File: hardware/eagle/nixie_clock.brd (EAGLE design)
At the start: 199.4 x 199.4 mm, 72 parts, among them IC1 74141N, IC10 7477N, IC11 74141N, IC12 7477N, IC2 7477N, IC3 74141N, IC4 7477N, IC5 74141N, IC6 7477N, IC7 74141N, IC8 7477N, IC9 74141N, J1 RASPBERRYPI-40-PIN-GPIO, J1_180V 22-27-2021-02, J1_5V1 22-27-2021-02, J1_5V2 22-27-2021-02, K1 4052, SW1 ROTARTY_ENCODER

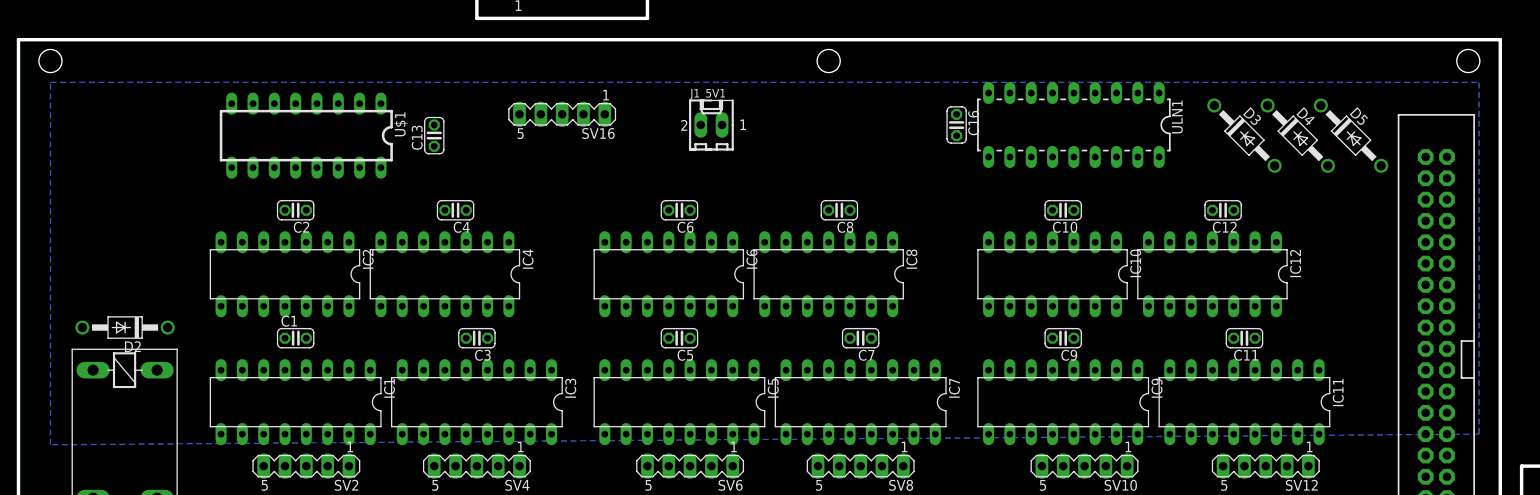
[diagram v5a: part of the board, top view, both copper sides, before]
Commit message: Fixed some issues related with the multiplexed data
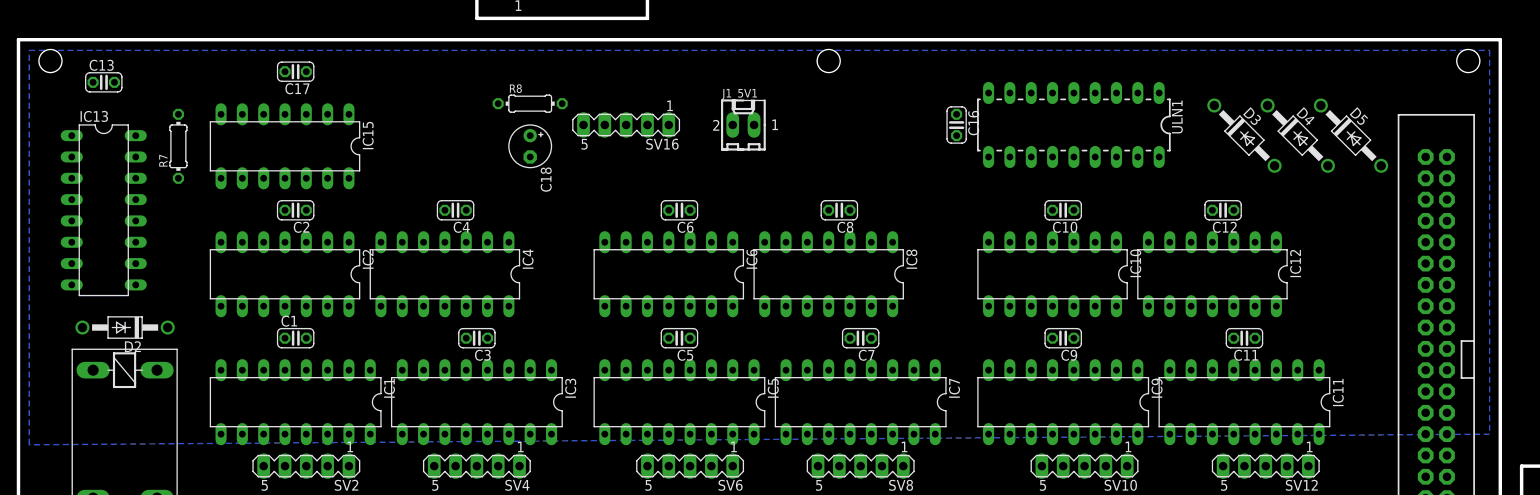
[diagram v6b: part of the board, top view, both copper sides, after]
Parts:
- removed U$1: M74HC238, SparkFun-DigitalIC:DIL16
- added C17: 100nF, resistor:C025-024X044
- added C18: 1uF, rcl:E2,5-5
- added IC13: 74HCT259N, 74xx-eu:DIL16
- added IC15: 7477N, 74xx-eu:DIL14
- added R7: 10k, rcl:0204/7
- added R8: 4k7, rcl:0204/7
- moved C13 39.9 mm to (10.2, 73.7), turned to 0 degrees
- moved SV16 7.73 mm to (72.4, 68.6)
- moved J1_5V1 3.81 mm to (86.4, 68.6)
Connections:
- removed net N$139: J1.10, ULN1.3
- new net N$141: IC15.1, J1.22
- new net N$142: IC15.2, J1.18
- new net N$143: IC15.5, J1.16
- new net N$144: IC15.6, J1.15
- new net N$145: C1.2, C10.2, C11.2, C12.2, C13.2, C16.2, C17.2, C2.2, C3.2, C4.2, C5.2, C6.2, C7.2, C8.2, C9.2, IC1.5, IC10.4, IC11.5, IC12.4, IC13.13, IC13.16, IC15.4, IC2.4, IC3.5, IC4.4, IC5.5, IC6.4, IC7.5, IC8.4, IC9.5, J1_5V1.2, R7.2, R8.1, SV16.1, ULN1.10
- new net N$146: IC15.12, IC15.3, J1.7, ULN1.4
- new net N$149: D2.C, J1.38, K1.1
- net GND: now also C13.1, C17.1, C18.-, IC13.8, IC15.11, SV16.2; no longer C13.2, U$1.4, U$1.5, U$1.8
- net N$124: now also J1.35, ULN1.1; no longer J1.26, SV16.5
- net N$127: now also J1.37, ULN1.2; no longer J1.19, SV16.4
- net N$129: now also J1.32, ULN1.3; no longer D2.C, J1.7, K1.1
- net N$130: now also C18.+, J1.33, R8.2; no longer J1.21
- net N$137: now also J1.31, SV16.5; no longer J1.23, ULN1.1
- net N$138: now also J1.29, SV16.4; no longer J1.8, ULN1.2
- net N$140: now also IC13.14, IC13.15, R7.1, ULN1.15; no longer C1.2, C10.2, C11.2, C12.2, C13.1, C16.2, C2.2, C3.2, C4.2, C5.2, C6.2, C7.2, C8.2, C9.2, IC1.5, IC10.4, IC11.5, IC12.4, IC2.4, IC3.5, IC4.4, IC5.5, IC6.4, IC7.5, IC8.4, IC9.5, J1_5V1.2, U$1.16, U$1.6, ULN1.10
- net N$16: now also IC13.4; no longer U$1.15
- net N$17: now also IC15.8; no longer J1.15
- net N$33: now also IC13.5; no longer U$1.14
- net N$48: now also IC13.6; no longer U$1.13
- net N$63: now also IC13.7; no longer U$1.12
- net N$78: now also IC13.9; no longer U$1.11
- net N$93: now also IC13.10; no longer U$1.10
- net N$94: now also IC15.9; no longer J1.16
- net N$95: now also IC15.13; no longer J1.18
- net N$96: now also IC15.14; no longer J1.22
- net N$97: now also IC13.1; no longer U$1.1
- net N$98: now also IC13.2; no longer U$1.2
- net N$99: now also IC13.3; no longer U$1.3

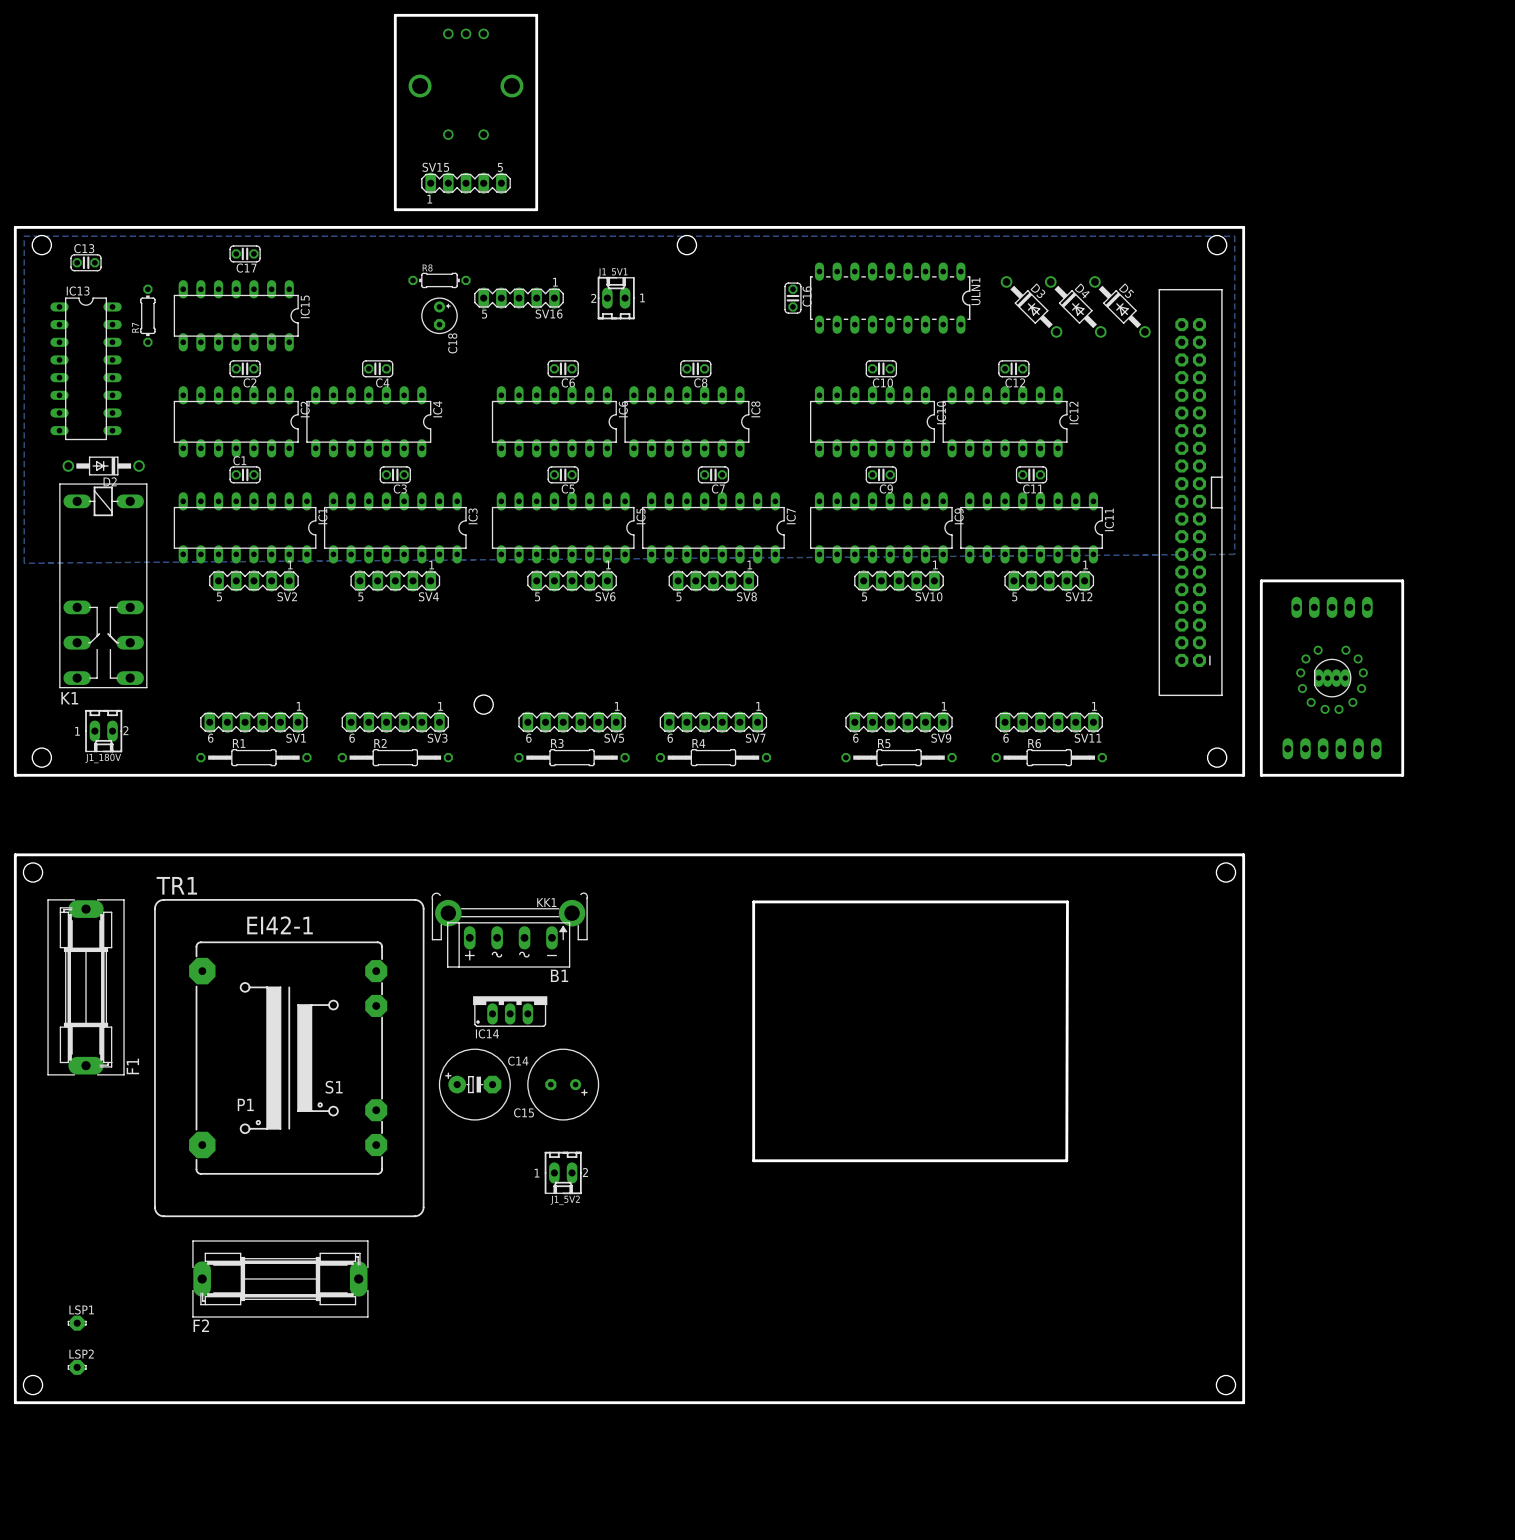
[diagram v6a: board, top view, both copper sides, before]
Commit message: Updated clock.c and removed rencoder test
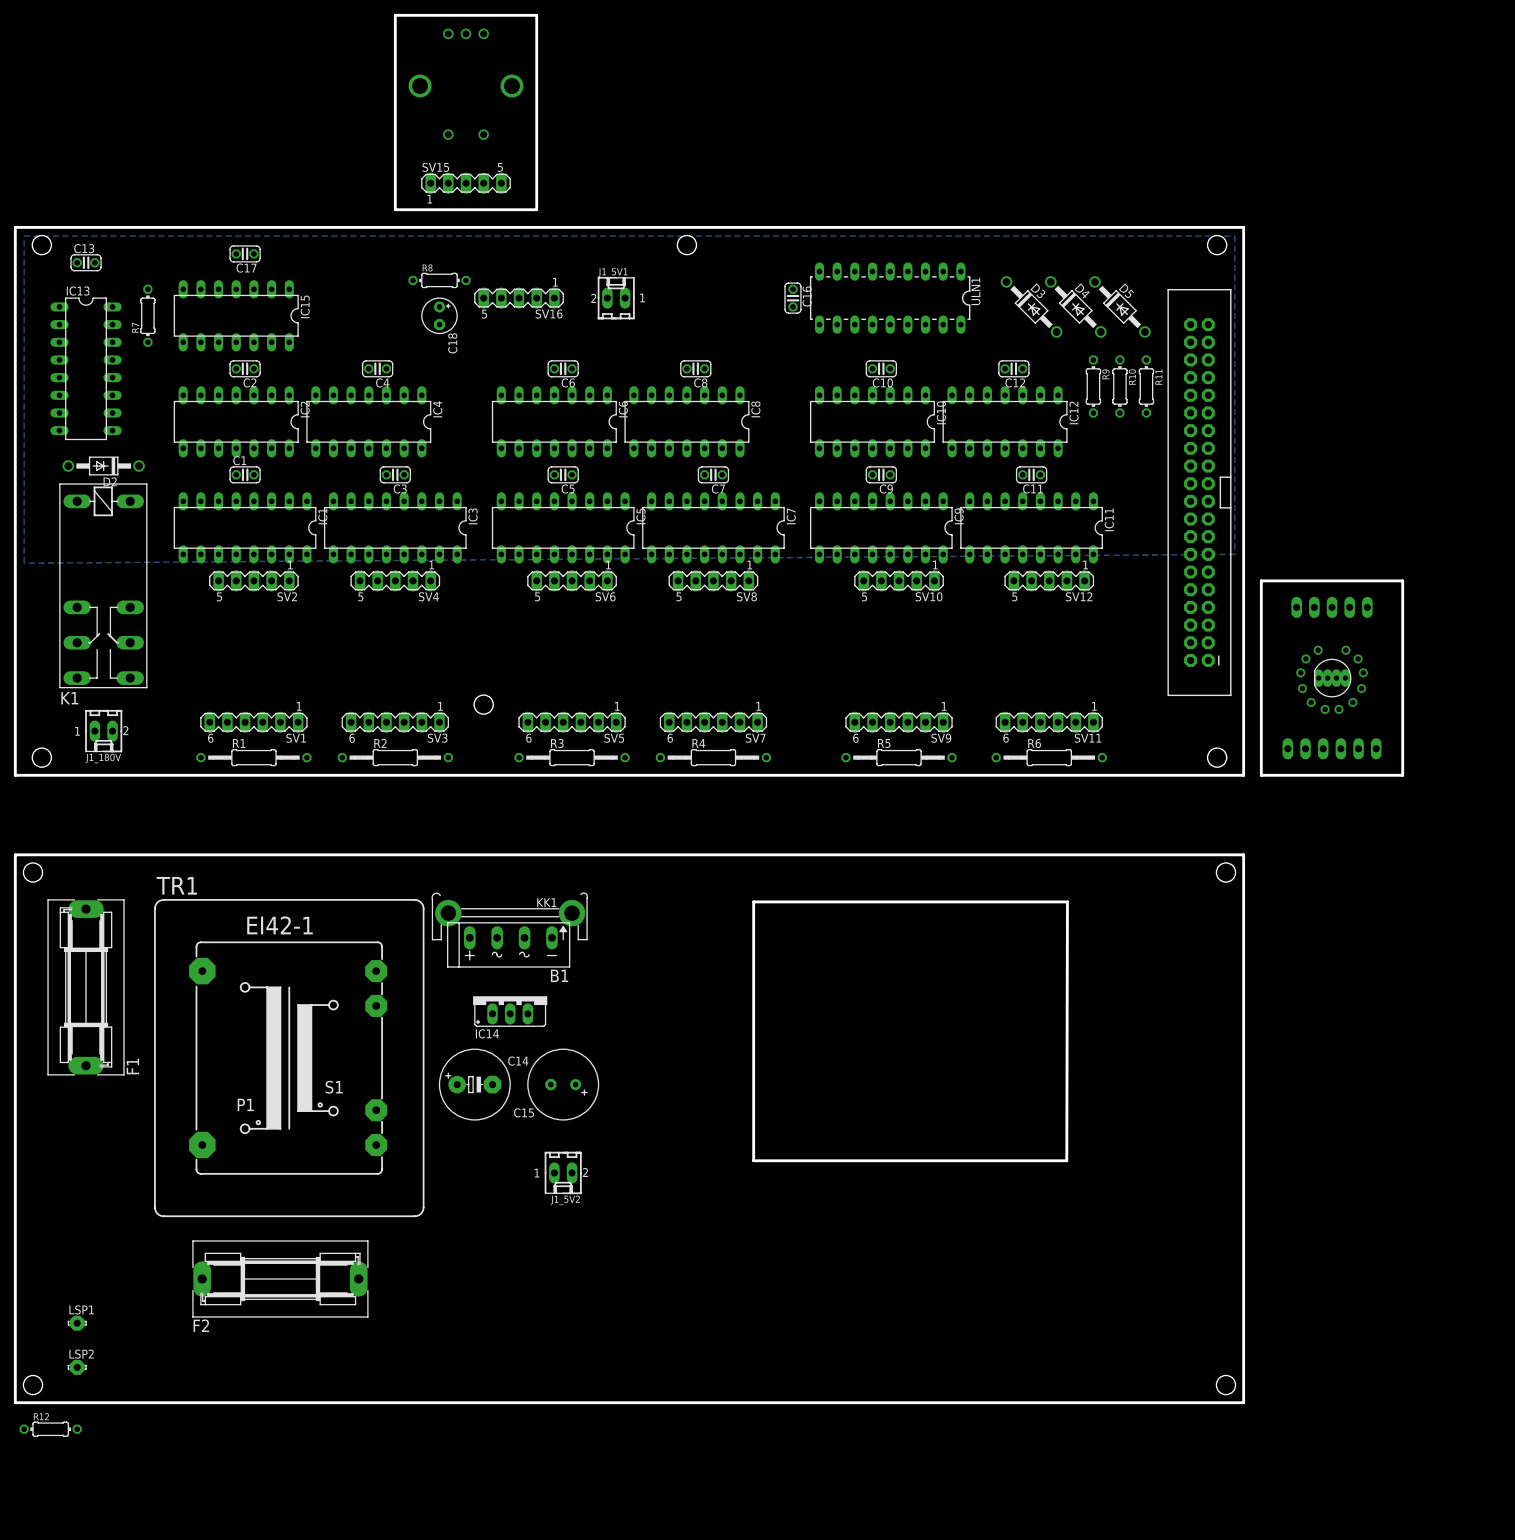
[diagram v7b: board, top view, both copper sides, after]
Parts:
- added R10, R11: 100, rcl:0204/7
- added R12: 10k, rcl:0204/7
- added R9: 150, rcl:0204/7
- moved J1 1.27 mm to (170.2, 40.6)
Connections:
- removed net N$145: C1.2, C10.2, C11.2, C12.2, C13.2, C16.2, C17.2, C2.2, C3.2, C4.2, C5.2, C6.2, C7.2, C8.2, C9.2, IC1.5, IC10.4, IC11.5, IC12.4, IC13.13, IC13.16, IC15.4, IC2.4, IC3.5, IC4.4, IC5.5, IC6.4, IC7.5, IC8.4, IC9.5, J1_5V1.2, R7.2, R8.1, SV16.1, ULN1.10
- new net N$139: D3.A, R9.1
- new net N$147: D4.A, R10.1
- new net N$148: D5.A, R11.1
- new net N$151: D2.C, K1.1, R12.1, ULN1.14
- new net N$152: C1.2, C10.2, C11.2, C12.2, C13.2, C16.2, C17.2, C2.2, C3.2, C4.2, C5.2, C6.2, C7.2, C8.2, C9.2, D2.A, IC1.5, IC10.4, IC11.5, IC12.4, IC13.13, IC13.16, IC15.4, IC2.4, IC3.5, IC4.4, IC5.5, IC6.4, IC7.5, IC8.4, IC9.5, J1_5V1.2, K1.2, R12.2, R7.2, R8.1, SV16.1, ULN1.10
- net GND: no longer D2.A, K1.2
- net N$149: now also ULN1.5; no longer D2.C, K1.1

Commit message: Fixed bug related to multiplexed data
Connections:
- net GND: now also IC13.15
- net N$140: no longer IC13.15
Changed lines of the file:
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@@
 <contactref element="SV16" pad="2"/>
 <contactref element="C18" pad="-"/>
+<contactref element="IC13" pad="15"/>
 <wire x1="168.91" y1="57.15" x2="171.45" y2="64.77" width="0" layer="19" extent="1-1"/>
 <wire x1="168.91" y1="52.07" x2="168.91" y2="57.15" width="0" layer="19" extent="1-1"/>
@@
 <wire x1="31.75" y1="31.75" x2="31.75" y2="43.18" width="0" layer="19" extent="1-1"/>
 <wire x1="34.29" y1="74.93" x2="31.75" y2="62.23" width="0" layer="19" extent="1-1"/>
-<wire x1="8.89" y1="73.66" x2="34.29" y2="74.93" width="0" layer="19" extent="1-1"/>
-<wire x1="6.35" y1="49.53" x2="8.89" y2="73.66" width="0" layer="19" extent="1-1"/>
+<wire x1="13.97" y1="64.77" x2="31.75" y2="62.23" width="0" layer="19" extent="1-1"/>
+<wire x1="8.89" y1="73.66" x2="13.97" y2="64.77" width="0" layer="19" extent="1-1"/>
+<wire x1="6.35" y1="49.53" x2="13.97" y2="64.77" width="0" layer="19" extent="1-1"/>
 <wire x1="11.43" y1="6.35" x2="31.75" y2="31.75" width="0" layer="19" extent="1-1"/>
 </signal>
@@
 </signal>
 <signal name="N$140">
-<contactref element="IC13" pad="14"/>
-<contactref element="IC13" pad="15"/>
 <contactref element="ULN1" pad="15"/>
 <contactref element="R7" pad="1"/>
+<contactref element="IC13" pad="14"/>
 <wire x1="19.05" y1="62.23" x2="128.27" y2="64.77" width="0" layer="19" extent="1-1"/>
 <wire x1="13.97" y1="62.23" x2="19.05" y2="62.23" width="0" layer="19" extent="1-1"/>
-<wire x1="13.97" y1="64.77" x2="13.97" y2="62.23" width="0" layer="19" extent="1-1"/>
 </signal>
 <signal name="N$146">
